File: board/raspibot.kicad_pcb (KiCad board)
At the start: 2 copper layers, 50 x 50 mm, 20 parts, among them IC1 ATTINY4313-P, IC2 L293D, P1 CONN_2, P2 CONN_2, P3 CONN_5, P4 CONN_5, P5 CONN_5, P6 CONN_2, U1 ULN2803, X1 CRYSTAL

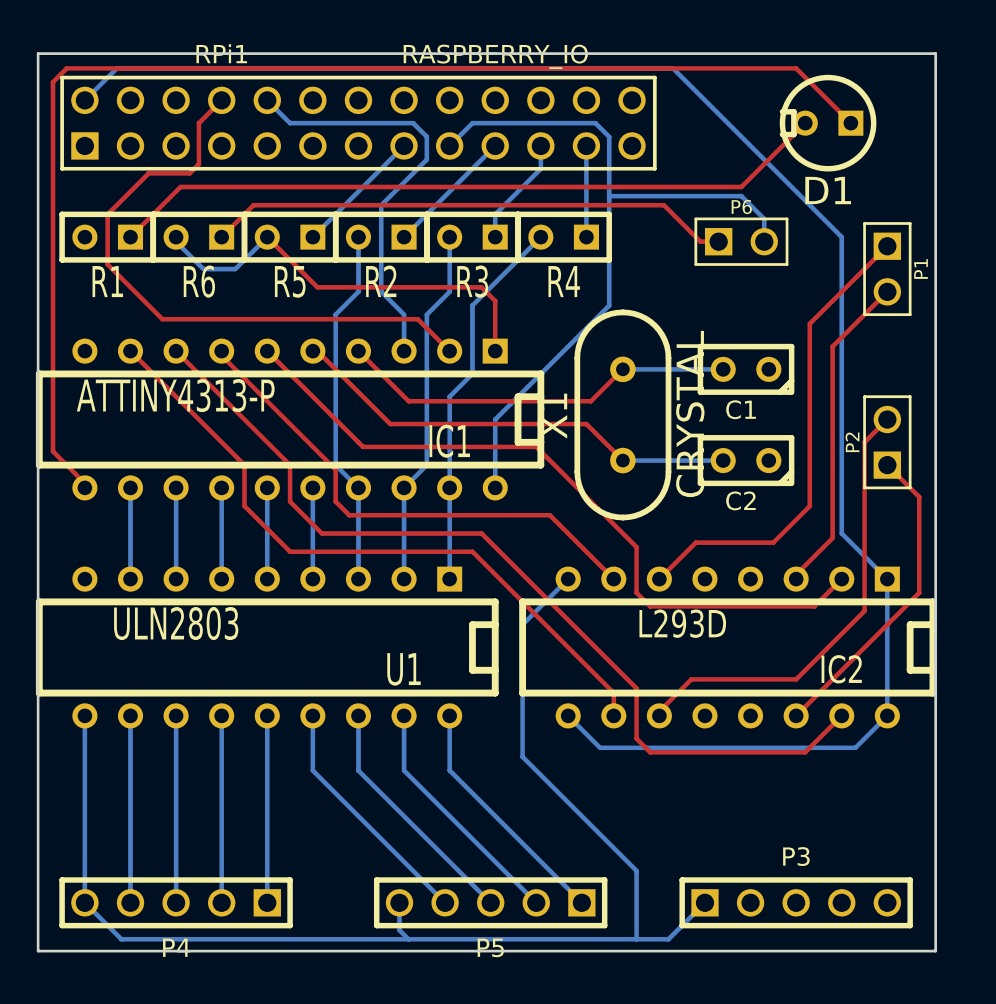
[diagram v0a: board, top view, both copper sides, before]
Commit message: Minor fixes, added URL to github repository
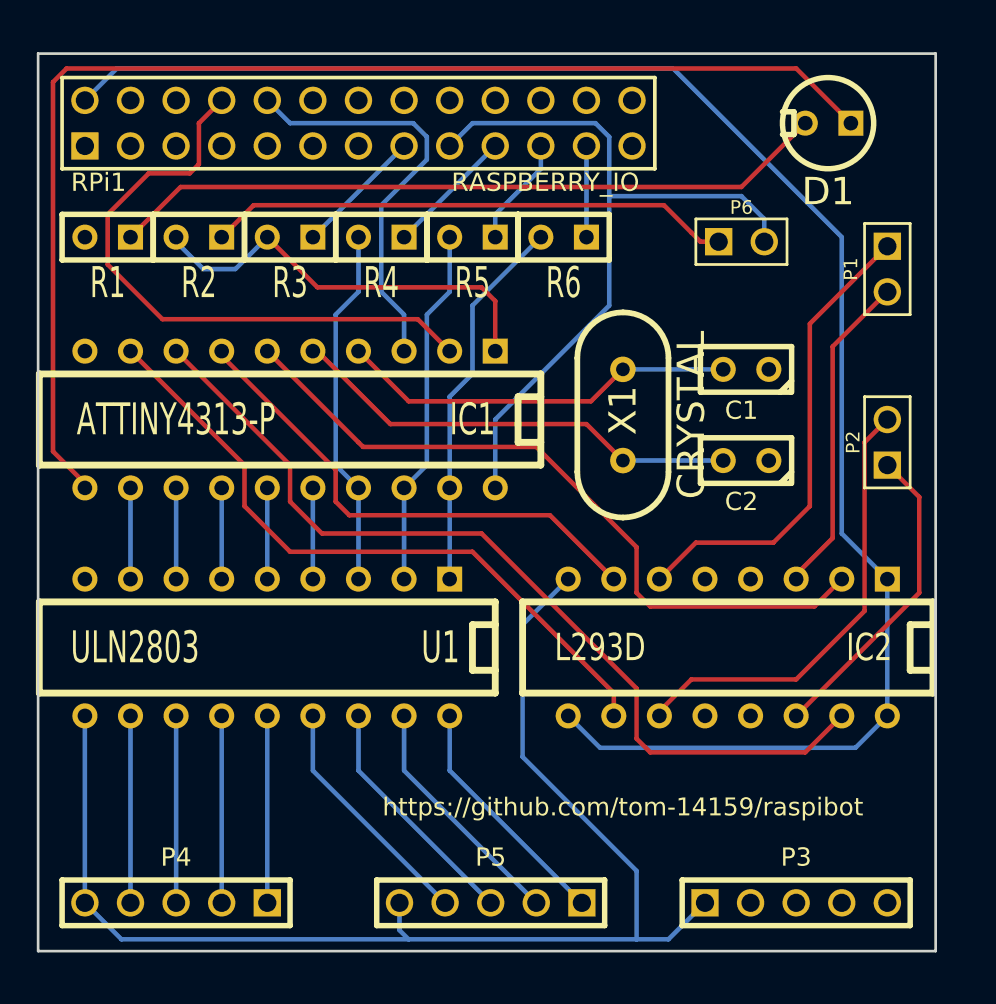
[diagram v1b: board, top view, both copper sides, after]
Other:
- board text added: "https://github.com/tom-14159/raspibot"
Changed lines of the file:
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@@
     (links 62)
     (no_connects 0)
-    (area 19.621499 19.2024 70.294501 70.7136)
+    (area 19.621499 19.924999 70.294501 70.7136)
     (thickness 1.6)
-    (drawings 4)
+    (drawings 5)
     (tracks 164)
     (zones 0)
@@
   (page A3)
   (layers
-    (15 F.Cu signal hide)
+    (15 F.Cu signal)
     (0 B.Cu signal)
-    (16 B.Adhes user)
-    (17 F.Adhes user)
-    (18 B.Paste user)
-    (19 F.Paste user)
+    (16 B.Adhes user hide)
+    (17 F.Adhes user hide)
+    (18 B.Paste user hide)
+    (19 F.Paste user hide)
     (20 B.SilkS user)
     (21 F.SilkS user)
-    (22 B.Mask user)
-    (23 F.Mask user)
+    (22 B.Mask user hide)
+    (23 F.Mask user hide)
     (24 Dwgs.User user)
-    (25 Cmts.User user)
-    (26 Eco1.User user)
-    (27 Eco2.User user)
-    (28 Edge.Cuts user)
+    (25 Cmts.User user hide)
+    (26 Eco1.User user hide)
+    (27 Eco2.User user hide)
+    (28 Edge.Cuts user hide)
   )
   (setup
@@
     (visible_elements FFFFFFBF)
     (pcbplotparams
-      (layerselection 3178497)
+      (layerselection 271613953)
       (usegerberextensions true)
       (excludeedgelayer true)
@@
       (outputformat 1)
       (mirror false)
-      (drillshape 1)
+      (drillshape 0)
       (scaleselection 1)
-      (outputdirectory ""))
+      (outputdirectory gerber/))
   )
   (net 0 "")
@@
     (descr "Connecteurs 2 pins")
     (tags "CONN DEV")
-    (fp_text reference R6 (at 0 -2.54 180) (layer F.SilkS)
+    (fp_text reference R6 (at -20.32 -2.54 180) (layer F.SilkS)
       (effects (font (size 1.72974 1.08712) (thickness 0.3048)))
     )
@@
     (descr "Connecteurs 2 pins")
     (tags "CONN DEV")
-    (fp_text reference R4 (at 0 -2.54 180) (layer F.SilkS)
+    (fp_text reference R4 (at 10.16 -2.54 180) (layer F.SilkS)
       (effects (font (size 1.72974 1.08712) (thickness 0.3048)))
     )
@@
     (descr "Connecteurs 2 pins")
     (tags "CONN DEV")
-    (fp_text reference R3 (at 0 -2.54 180) (layer F.SilkS)
+    (fp_text reference R3 (at 10.16 -2.54 180) (layer F.SilkS)
       (effects (font (size 1.72974 1.08712) (thickness 0.3048)))
     )
@@
     (descr "Connecteurs 2 pins")
     (tags "CONN DEV")
-    (fp_text reference R2 (at 0 -2.54 180) (layer F.SilkS)
+    (fp_text reference R2 (at 10.16 -2.54 180) (layer F.SilkS)
       (effects (font (size 1.72974 1.08712) (thickness 0.3048)))
     )
@@
     (descr "Connecteurs 2 pins")
     (tags "CONN DEV")
-    (fp_text reference R5 (at 0 -2.54 180) (layer F.SilkS)
+    (fp_text reference R5 (at -10.16 -2.54 180) (layer F.SilkS)
       (effects (font (size 1.72974 1.08712) (thickness 0.3048)))
     )
@@
     (descr "Double rangee de contacts 2 x 5 pins")
     (tags CONN)
-    (fp_text reference P4 (at 0 -2.54 180) (layer F.SilkS)
+    (fp_text reference P4 (at 0 2.54 180) (layer F.SilkS)
       (effects (font (size 1.016 1.016) (thickness 0.2032)))
     )
@@
     (descr "Double rangee de contacts 2 x 5 pins")
     (tags CONN)
-    (fp_text reference P5 (at 0 -2.54 180) (layer F.SilkS)
+    (fp_text reference P5 (at 0 2.54 180) (layer F.SilkS)
       (effects (font (size 1.016 1.016) (thickness 0.2032)))
     )
@@
     (descr "Connecteurs 2 pins")
     (tags "CONN DEV")
-    (fp_text reference P1 (at 0 -1.905 270) (layer F.SilkS)
+    (fp_text reference P1 (at 0 2.032 270) (layer F.SilkS)
       (effects (font (size 0.762 0.762) (thickness 0.1524)))
     )
@@
     (descr "2 x 13 pins connector")
     (tags CONN)
-    (fp_text reference RPi1 (at -7.62 -3.81) (layer F.SilkS)
+    (fp_text reference RPi1 (at -14.478 3.302) (layer F.SilkS)
       (effects (font (size 1.016 1.016) (thickness 0.2032)))
     )
-    (fp_text value RASPBERRY_IO (at 7.62 -3.81) (layer F.SilkS)
+    (fp_text value RASPBERRY_IO (at 10.414 3.302) (layer F.SilkS)
       (effects (font (size 1.016 1.016) (thickness 0.2032)))
     )
@@
     (tags "QUARTZ DEV")
     (autoplace_cost180 10)
-    (fp_text reference X1 (at 0 -3.81 90) (layer F.SilkS)
+    (fp_text reference X1 (at 0.254 0 90) (layer F.SilkS)
       (effects (font (size 1.524 1.524) (thickness 0.3048)))
     )
@@
     (descr "20 pins DIL package, round pads")
     (tags DIL)
-    (fp_text reference IC1 (at -8.89 -1.27 180) (layer F.SilkS)
+    (fp_text reference IC1 (at -10.16 0 180) (layer F.SilkS)
       (effects (font (size 1.778 1.143) (thickness 0.3048)))
     )
-    (fp_text value ATTINY4313-P (at 6.35 1.27 180) (layer F.SilkS)
+    (fp_text value ATTINY4313-P (at 6.35 0 180) (layer F.SilkS)
       (effects (font (size 1.778 1.143) (thickness 0.3048)))
     )
@@
     (at 32.766 53.086 180)
     (descr "8 pins DIL package, round pads")
-    (fp_text reference U1 (at -7.62 -1.27 180) (layer F.SilkS)
+    (fp_text reference U1 (at -9.652 0 180) (layer F.SilkS)
       (effects (font (size 1.778 1.143) (thickness 0.3048)))
     )
-    (fp_text value ULN2803 (at 5.08 1.27 180) (layer F.SilkS)
+    (fp_text value ULN2803 (at 7.366 0 180) (layer F.SilkS)
       (effects (font (size 1.778 1.143) (thickness 0.3048)))
     )
@@
     (descr "16 pins DIL package, round pads")
     (tags DIL)
-    (fp_text reference IC2 (at -6.35 -1.27 180) (layer F.SilkS)
+    (fp_text reference IC2 (at -7.874 0 180) (layer F.SilkS)
       (effects (font (size 1.524 1.143) (thickness 0.3048)))
     )
-    (fp_text value L293D (at 2.54 1.27 180) (layer F.SilkS)
+    (fp_text value L293D (at 7.112 0 180) (layer F.SilkS)
       (effects (font (size 1.524 1.143) (thickness 0.3048)))
     )
@@
       (rotate (xyz 0 0 0))
     )
+  )
+  (gr_text https://github.com/tom-14159/raspibot (at 52.578 61.976) (layer F.SilkS)
+    (effects (font (size 1 1) (thickness 0.25)))
   )
   (gr_line (start 20 70) (end 20 20) (angle 90) (layer Edge.Cuts) (width 0.15))
@@
   (segment (start 35.306 49.276) (end 35.306 44.196) (width 0.254) (layer B.Cu) (net 10))
   (segment (start 25.146 49.276) (end 25.146 44.196) (width 0.254) (layer B.Cu) (net 11))
-  (segment (start 60.452 30.48) (end 60.452 29.21) (width 0.254) (layer B.Cu) (net 12) (status 400000))
+  (segment (start 60.452 30.48) (end 60.452 29.21) (width 0.254) (layer B.Cu) (net 12))
   (segment (start 59.182 27.94) (end 51.816 27.94) (width 0.254) (layer B.Cu) (net 12))
   (segment (start 60.452 29.21) (end 59.182 27.94) (width 0.254) (layer B.Cu) (net 12))
@@
   (segment (start 54.864 28.448) (end 56.388 29.972) (width 0.254) (layer F.Cu) (net 25))
   (segment (start 30.226 30.226) (end 32.004 28.448) (width 0.254) (layer F.Cu) (net 25))
-  (segment (start 56.896 30.48) (end 57.912 30.48) (width 0.254) (layer F.Cu) (net 25) (status 800000))
+  (segment (start 56.896 30.48) (end 57.912 30.48) (width 0.254) (layer F.Cu) (net 25))
   (segment (start 28.956 23.876) (end 28.956 26.162) (width 0.254) (layer F.Cu) (net 26))
   (segment (start 30.226 22.606) (end 28.956 23.876) (width 0.254) (layer F.Cu) (net 26))
